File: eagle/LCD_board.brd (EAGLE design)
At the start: 5 parts, among them CN1 1X4-CLEANBIG

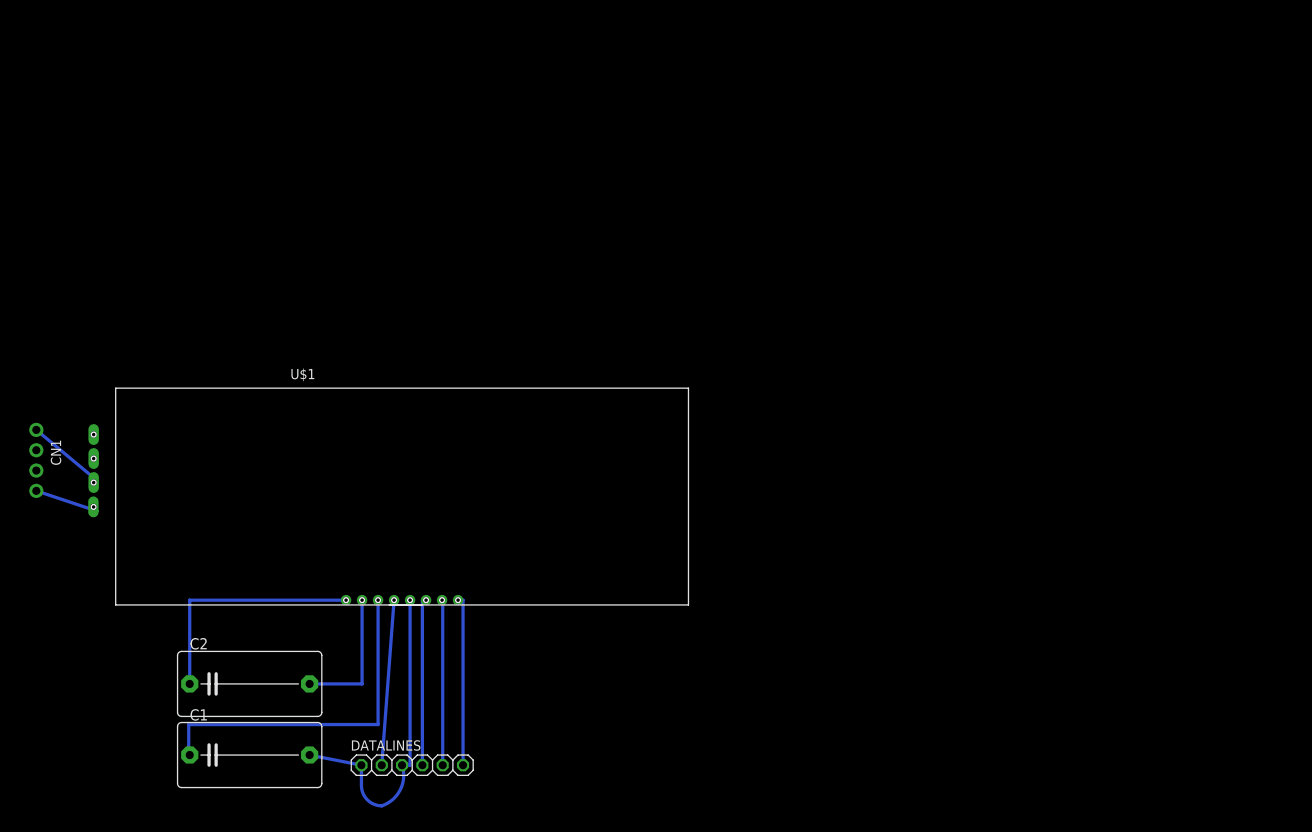
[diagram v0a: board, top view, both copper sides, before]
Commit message: Moved ARGB pins on LCD screen schematic to match physical location. This should solve issue #9. Updated LCD_board.sch to reflect these changes.
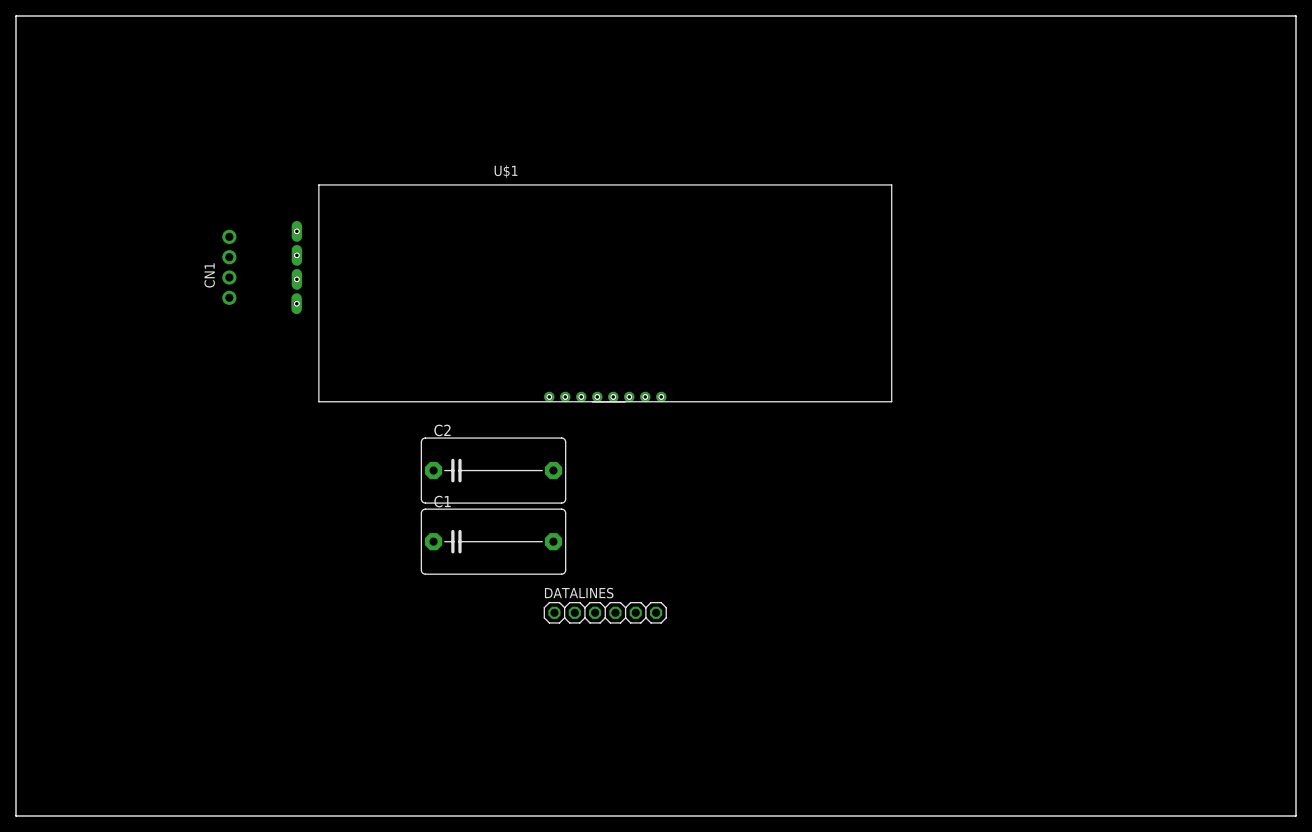
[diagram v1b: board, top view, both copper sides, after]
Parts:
- moved C1 40.5 mm to (59.7, 34.3)
- moved C2 40.5 mm to (59.7, 43.2)
- moved U$1 35.9 mm to (73.7, 68.6)
- moved CN1 34.1 mm to (26.7, 68.6), turned to 90 degrees
- moved DATALINES 30.7 mm to (73.7, 25.4)
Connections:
- net A: now also U$1.P$RK; no longer U$1.P$A
- net GK: now also U$1.P$BK; no longer U$1.P$GK
- net N$2: now also U$1.P$GK; no longer U$1.P$RK
- net N$4: now also U$1.P$A; no longer U$1.P$BK
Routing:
- net N$3: track 43.2 -> 0.00 mm
- net GND: track 40.0 -> 0.00 mm
- net N$1: track 30.0 -> 0.00 mm
- net RST: track 21.3 -> 0.00 mm
- net SDA: track 21.1 -> 0.00 mm
- net SCL: track 20.7 -> 0.00 mm
- net VDD: track 20.7 -> 0.00 mm
- net C1+: track 17.0 -> 0.00 mm
- net N$4: track 9.92 -> 0.00 mm
- net A: track 8.03 -> 0.00 mm
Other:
- board outline added: 160 x 100 mm
